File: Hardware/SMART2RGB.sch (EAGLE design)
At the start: 11 parts, among them IC1 WS2811-SOP8, IC2 WS2811-SOP8, IC3 WS2811-SOP8, SW1 QG16F-RGB, SW2 QG16F-RGB, SW3 QG16F-RGB

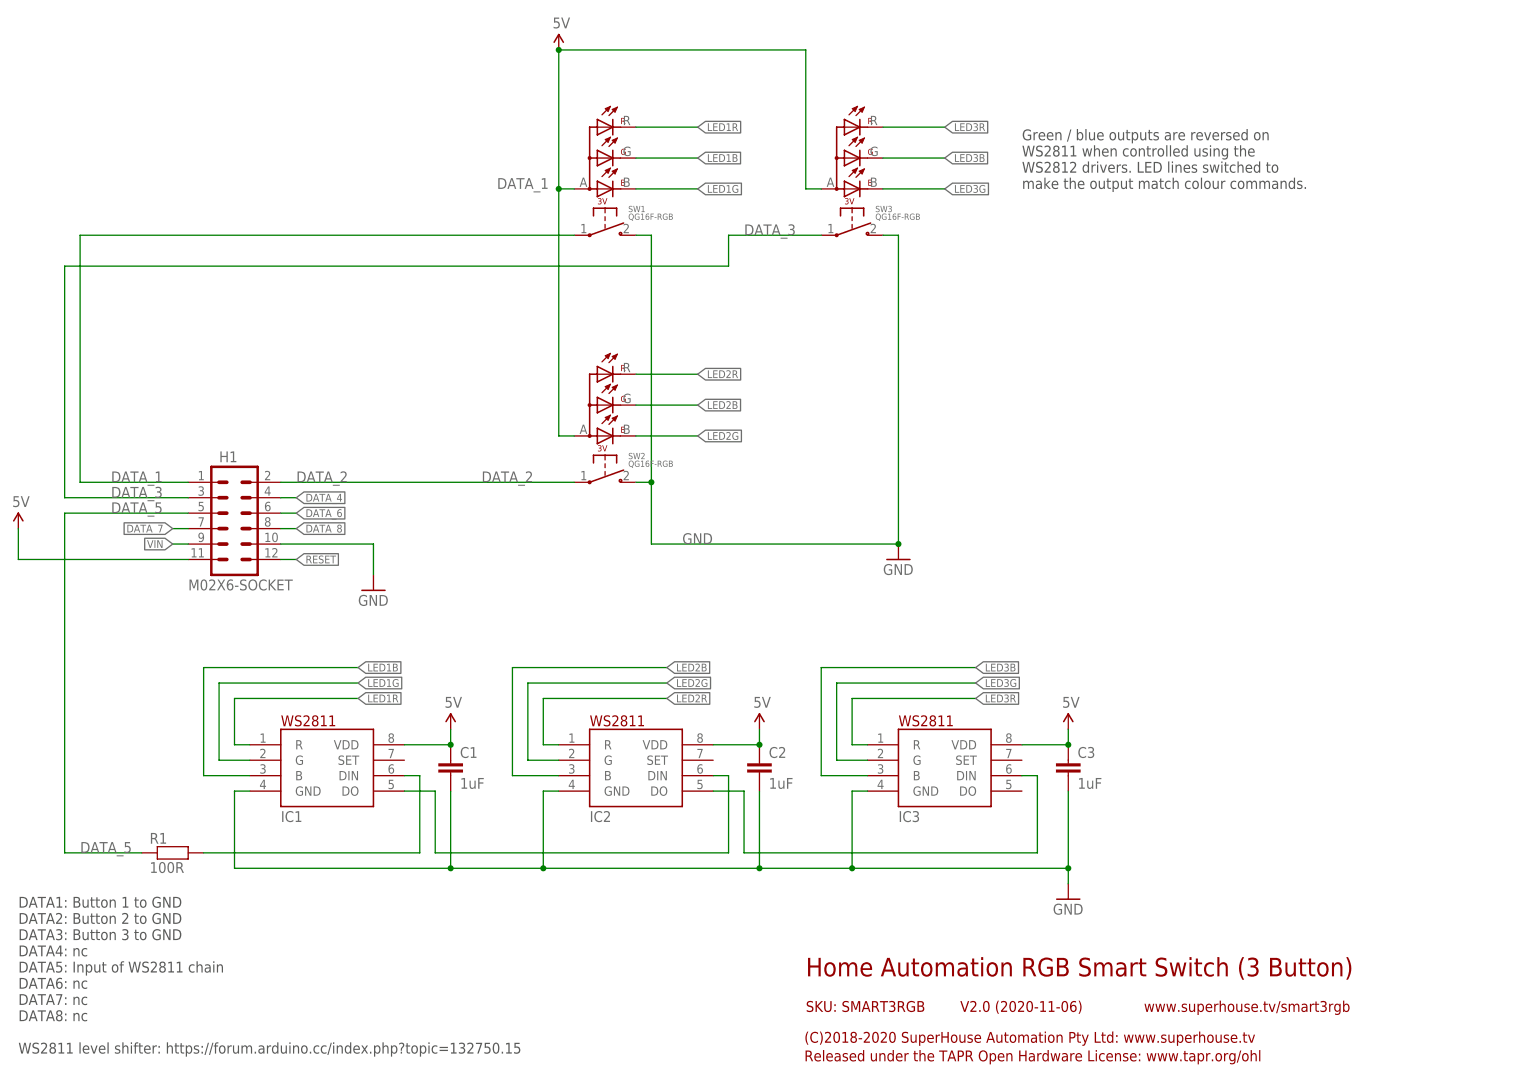
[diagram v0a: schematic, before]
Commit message: Final routing, ERC, and DRC for v2.0 release.
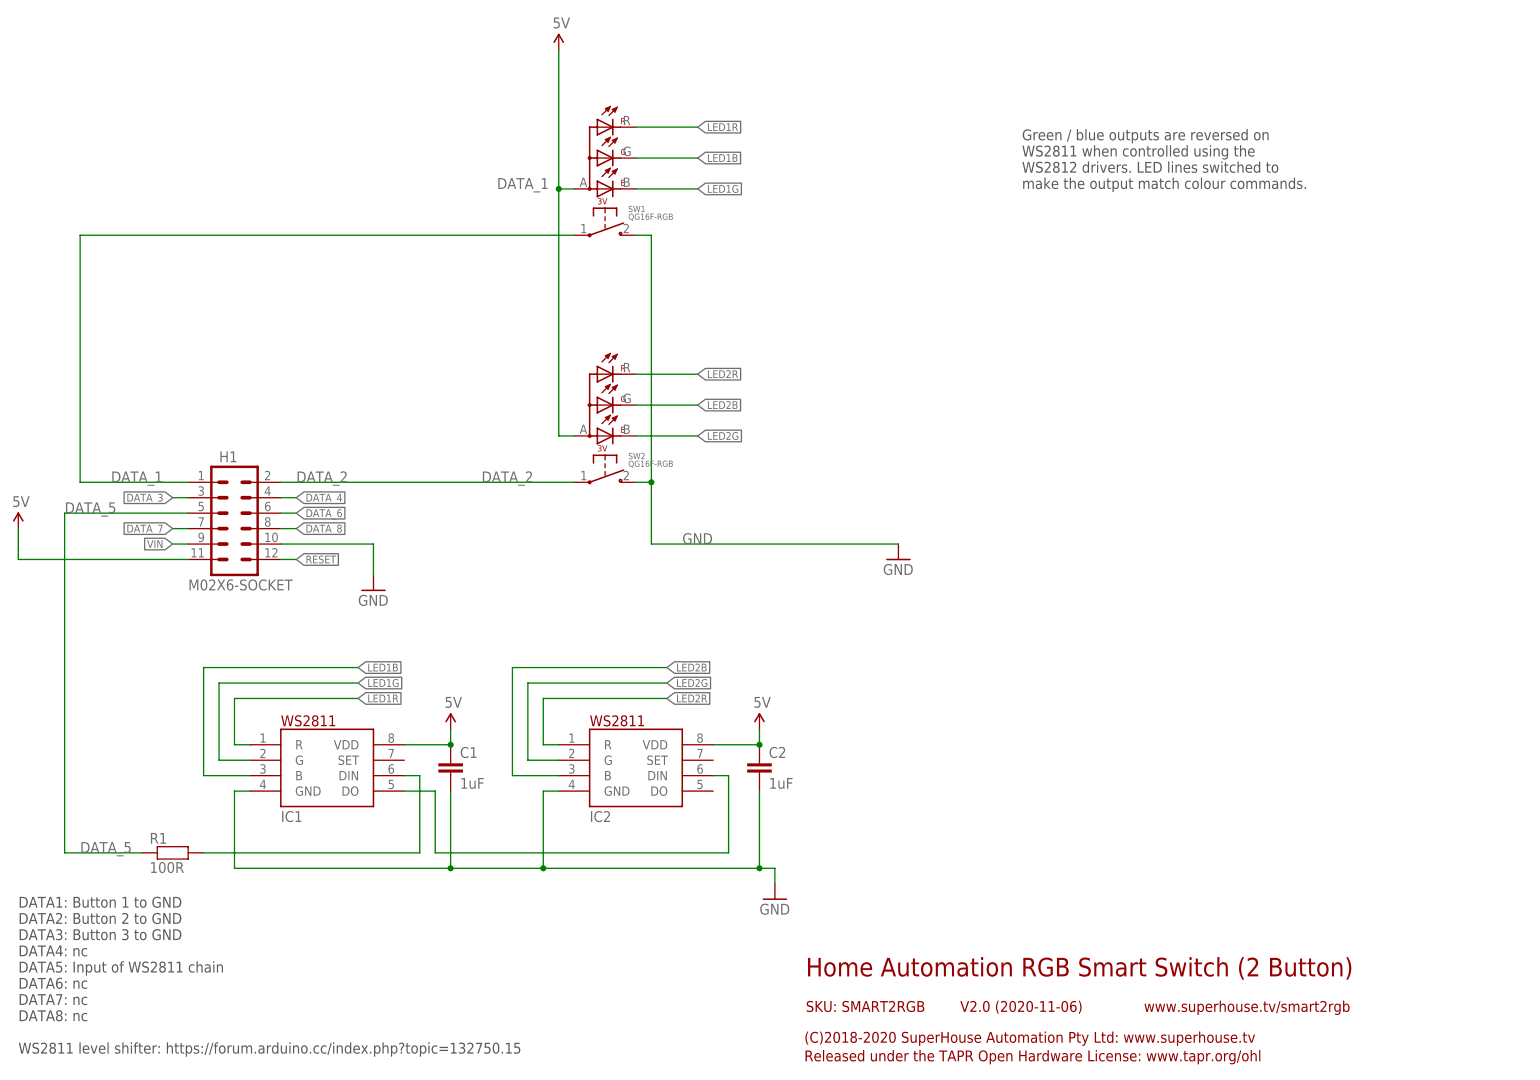
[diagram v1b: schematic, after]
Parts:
- removed C3: 1uF, SuperHouse-DiscreteSemi:CAP0603
- removed IC3: WS2811-SOP8, SuperHouse-ICs:WS2811-SOP8
- removed SW3: QG16F-RGB, SuperHouse-Switches:QG16F-RGB
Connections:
- removed net LED3B: IC3.B, SW3.G
- removed net LED3G: IC3.G, SW3.B
- removed net LED3R: IC3.R, SW3.R
- removed net N$12: IC2.DO, IC3.DIN
- net 5V: no longer C3.1, IC3.VDD, SW3.+
- net DATA_3: no longer SW3.1
- net GND: no longer C3.2, IC3.GND, SW3.2
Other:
- note added: "Home Automation RGB Smart Switch (2 Button)"
- note added: "SKU: SMART2RGB"
- note added: "www.superhouse.tv/smart2rgb"
- note removed: "Home Automation RGB Smart Switch (3 Button)"
- note removed: "SKU: SMART3RGB"
- note removed: "www.superhouse.tv/smart3rgb"

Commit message: Converted switch isolation from FETs to diodes for v2.1 release.
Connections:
- net LED1B: now also SW1.B; no longer SW1.G
- net LED1G: now also IC1.R, SW1.G; no longer IC1.G, SW1.B
- net LED1R: now also IC1.G; no longer IC1.R
- net LED2B: now also SW2.B; no longer SW2.G
- net LED2G: now also IC2.R, SW2.G; no longer IC2.G, SW2.B
- net LED2R: now also IC2.G; no longer IC2.R
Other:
- note added: "Colours are mismatched on WS2811 when controlled using the WS2812 drivers. LED lines switched to make the output match colour commands."
- note added: "V2.1 (2020-12-23)"
- note removed: "Green / blue outputs are reversed on WS2811 when controlled using the WS2812 drivers. LED lines switched to make the output match colour commands."
- note removed: "V2.0 (2020-11-06)"
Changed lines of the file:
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@@
 <frame x1="0" y1="0" x2="248.92" y2="185.42" columns="8" rows="5" layer="94"/>
 <text x="139.7" y="20.32" size="3.048" layer="94">Home Automation RGB Smart Switch (2 Button)</text>
-<text x="165.1" y="14.478" size="1.778" layer="94">V2.0 (2020-11-06)</text>
+<text x="165.1" y="14.478" size="1.778" layer="94">V2.1 (2020-12-23)</text>
 <text x="139.7" y="14.478" size="1.778" layer="94">SKU: SMART2RGB</text>
 <text x="139.446" y="9.398" size="1.778" layer="94">(C)2018-2020 SuperHouse Automation Pty Ltd: www.superhouse.tv</text>
@@
 DATA8: nc
 WS2811 level shifter: https://forum.arduino.cc/index.php?topic=132750.15</text>
-<text x="175.26" y="149.86" size="1.778" layer="97">Green / blue outputs are reversed on
+<text x="175.26" y="149.86" size="1.778" layer="97">Colours are mismatched on
 WS2811 when controlled using the
 WS2812 drivers. LED lines switched to
@@
 </segment>
 <segment>
-<pinref part="SW1" gate="G$1" pin="G"/>
-<wire x1="111.76" y1="154.94" x2="121.92" y2="154.94" width="0.1524" layer="91"/>
-<label x="121.92" y="154.94" size="1.27" layer="95" xref="yes"/>
+<wire x1="111.76" y1="149.86" x2="121.92" y2="149.86" width="0.1524" layer="91"/>
+<pinref part="SW1" gate="G$1" pin="B"/>
+<label x="121.92" y="149.86" size="1.27" layer="95" xref="yes"/>
 </segment>
 </net>
@@
 </segment>
 <segment>
-<pinref part="SW2" gate="G$1" pin="G"/>
-<wire x1="111.76" y1="114.3" x2="121.92" y2="114.3" width="0.1524" layer="91"/>
-<label x="121.92" y="114.3" size="1.27" layer="95" xref="yes"/>
+<wire x1="111.76" y1="109.22" x2="121.92" y2="109.22" width="0.1524" layer="91"/>
+<pinref part="SW2" gate="G$1" pin="B"/>
+<label x="121.92" y="109.22" size="1.27" layer="95" xref="yes"/>
 </segment>
 </net>
@@
 </segment>
 <segment>
+<pinref part="IC1" gate="G$1" pin="G"/>
+<wire x1="48.26" y1="55.88" x2="43.18" y2="55.88" width="0.1524" layer="91"/>
+<wire x1="43.18" y1="55.88" x2="43.18" y2="68.58" width="0.1524" layer="91"/>
+<wire x1="43.18" y1="68.58" x2="66.04" y2="68.58" width="0.1524" layer="91"/>
+<label x="66.04" y="68.58" size="1.27" layer="95" xref="yes"/>
+</segment>
+</net>
+<net name="LED1G" class="0">
+<segment>
+<pinref part="SW1" gate="G$1" pin="G"/>
+<wire x1="111.76" y1="154.94" x2="121.92" y2="154.94" width="0.1524" layer="91"/>
+<label x="121.92" y="154.94" size="1.27" layer="95" xref="yes"/>
+</segment>
+<segment>
 <pinref part="IC1" gate="G$1" pin="R"/>
 <wire x1="48.26" y1="58.42" x2="45.72" y2="58.42" width="0.1524" layer="91"/>
@@
 </segment>
 </net>
-<net name="LED1G" class="0">
-<segment>
-<pinref part="IC1" gate="G$1" pin="G"/>
-<wire x1="48.26" y1="55.88" x2="43.18" y2="55.88" width="0.1524" layer="91"/>
-<wire x1="43.18" y1="55.88" x2="43.18" y2="68.58" width="0.1524" layer="91"/>
-<wire x1="43.18" y1="68.58" x2="66.04" y2="68.58" width="0.1524" layer="91"/>
-<label x="66.04" y="68.58" size="1.27" layer="95" xref="yes"/>
-</segment>
-<segment>
-<wire x1="111.76" y1="149.86" x2="121.92" y2="149.86" width="0.1524" layer="91"/>
-<pinref part="SW1" gate="G$1" pin="B"/>
-<label x="121.92" y="149.86" size="1.27" layer="95" xref="yes"/>
-</segment>
-</net>
 <net name="LED2G" class="0">
+<segment>
+<pinref part="SW2" gate="G$1" pin="G"/>
+<wire x1="111.76" y1="114.3" x2="121.92" y2="114.3" width="0.1524" layer="91"/>
+<label x="121.92" y="114.3" size="1.27" layer="95" xref="yes"/>
+</segment>
+<segment>
+<pinref part="IC2" gate="G$1" pin="R"/>
+<wire x1="99.06" y1="58.42" x2="96.52" y2="58.42" width="0.1524" layer="91"/>
+<wire x1="96.52" y1="58.42" x2="96.52" y2="66.04" width="0.1524" layer="91"/>
+<wire x1="96.52" y1="66.04" x2="116.84" y2="66.04" width="0.1524" layer="91"/>
+<label x="116.84" y="66.04" size="1.27" layer="95" xref="yes"/>
+</segment>
+</net>
+<net name="LED2R" class="0">
+<segment>
+<pinref part="SW2" gate="G$1" pin="R"/>
+<wire x1="111.76" y1="119.38" x2="121.92" y2="119.38" width="0.1524" layer="91"/>
+<label x="121.92" y="119.38" size="1.27" layer="95" xref="yes"/>
+</segment>
 <segment>
 <pinref part="IC2" gate="G$1" pin="G"/>
@@
 <label x="116.84" y="68.58" size="1.27" layer="95" xref="yes"/>
 </segment>
-<segment>
-<wire x1="111.76" y1="109.22" x2="121.92" y2="109.22" width="0.1524" layer="91"/>
-<pinref part="SW2" gate="G$1" pin="B"/>
-<label x="121.92" y="109.22" size="1.27" layer="95" xref="yes"/>
-</segment>
-</net>
-<net name="LED2R" class="0">
-<segment>
-<pinref part="SW2" gate="G$1" pin="R"/>
-<wire x1="111.76" y1="119.38" x2="121.92" y2="119.38" width="0.1524" layer="91"/>
-<label x="121.92" y="119.38" size="1.27" layer="95" xref="yes"/>
-</segment>
-<segment>
-<pinref part="IC2" gate="G$1" pin="R"/>
-<wire x1="99.06" y1="58.42" x2="96.52" y2="58.42" width="0.1524" layer="91"/>
-<wire x1="96.52" y1="58.42" x2="96.52" y2="66.04" width="0.1524" layer="91"/>
-<wire x1="96.52" y1="66.04" x2="116.84" y2="66.04" width="0.1524" layer="91"/>
-<label x="116.84" y="66.04" size="1.27" layer="95" xref="yes"/>
-</segment>
-</net>
+</net>
